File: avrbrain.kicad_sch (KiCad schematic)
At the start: 45 parts, among them J1 XKTF-0803-0, J12 PD/PE, J2 U254-051T-4BH81-S2S, J3 SM04B-SRSS-TB, J4 UPDI, J5 UEXT, J6 PIHAT, J7 PG/PB, J9 SM04B-SRSS-TB, Q1 BSS138, Q2 BSS138, SW1 RESET, U1 CH340C, U2 AVR128DB64x-xPT, U3 PCF8563T, U5 AMS1117-3.3, Y1 32kHz

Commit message: Tweaks to layout, finish all connections
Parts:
- removed J3: SM04B-SRSS-TB, Custom:JST_SM04B-SRSS-TB_LF__SN_, symbol Connector_Generic:Conn_01x04
- removed J6: PIHAT, Connector_PinHeader_2.54mm:PinHeader_2x13_P2.54mm_Vertical, symbol Connector_Generic:Conn_02x13_Odd_Even
- removed Q2: BSS138, Package_TO_SOT_SMD:SOT-23, symbol Transistor_FET:BSS138
- removed R2: 100K, Resistor_SMD:R_0402_1005Metric, symbol Device:R_Small
- removed Y1: 32kHz, Crystal:Crystal_SMD_3215-2Pin_3.2x1.5mm, symbol Device:Crystal_Small
- added J6: PC, Connector_PinHeader_2.54mm:PinHeader_2x10_P2.54mm_Vertical, symbol Connector_Generic:Conn_02x10_Odd_Even
- added J8: PG, Connector_PinHeader_2.54mm:PinHeader_2x10_P2.54mm_Vertical, symbol Connector_Generic:Conn_02x10_Odd_Even
- added JP1: AUTORESET, Jumper:SolderJumper-2_P1.3mm_Bridged_Pad1.0x1.5mm, symbol Jumper:Jumper_2_Bridged
- added JP2: CLK32K, Jumper:SolderJumper-2_P1.3mm_Bridged_Pad1.0x1.5mm, symbol Jumper:Jumper_2_Bridged
- added JP3: RTCINT, Jumper:SolderJumper-2_P1.3mm_Bridged_Pad1.0x1.5mm, symbol Jumper:Jumper_2_Bridged
- added SW2: VDD, SamacSys_Parts:JS202011CQN, symbol Switch:SW_SPDT
- J12: now not fitted
- J7: value PG/PB -> PA/PB; now not fitted
- renumbered D3 to D2, D2 to D3
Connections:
- net +3.3V: now also D2.2 (A), J1.P4 (VDD), J6.1 (Pin_1), J6.19 (Pin_19), SW2.3 (C), SW2.6 (C); no longer J1.P5 (CLK)
- net +5V: now also SW2.1 (A), SW2.4 (A)
- net CLK32K: now also JP2.1 (A); no longer U3.7 (CLKO)
- net GND: now also C6.2, J1.P6 (VSS), J4.3 (Pin_3), J6.10 (Pin_10), J6.12 (Pin_12), J6.14 (Pin_14), J6.16 (Pin_16), J6.18 (Pin_18), J6.2 (Pin_2), J6.20 (Pin_20), J6.4 (Pin_4), J6.6 (Pin_6), J6.8 (Pin_8), J8.10 (Pin_10), J8.12 (Pin_12), J8.14 (Pin_14), J8.16 (Pin_16), J8.18 (Pin_18), J8.2 (Pin_2), J8.20 (Pin_20), J8.4 (Pin_4), J8.6 (Pin_6), J8.8 (Pin_8); no longer J1.P7 (DAT0)
- net MISO: now also J1.P7 (DAT0), J6.11 (Pin_11); no longer J1.P8 (DAT1)
- net MOSI: now also J1.P3 (CMD), J6.13 (Pin_13); no longer J1.P4 (VDD)
- net PG0: now also J8.3 (Pin_3); no longer J7.4 (Pin_4)
- net PG1: now also J8.5 (Pin_5); no longer J7.6 (Pin_6)
- net PG2: now also J8.7 (Pin_7); no longer J7.8 (Pin_8)
- net PG3: now also J8.9 (Pin_9); no longer J7.10 (Pin_10)
- net PG4: now also J8.11 (Pin_11); no longer J7.12 (Pin_12)
- net PG5: now also J8.13 (Pin_13); no longer J7.14 (Pin_14)
- net PG6: now also J8.15 (Pin_15); no longer J7.16 (Pin_16)
- net PG7: now also J8.17 (Pin_17); no longer J7.18 (Pin_18)
- net RX3V: now also J6.5 (Pin_5)
- net SCK: now also J1.P5 (CLK), J6.15 (Pin_15); no longer J1.P6 (VSS)
- net TX3V: now also J6.3 (Pin_3)
- net VDD: now also C6.1, J4.2 (Pin_2), J8.1 (Pin_1), J8.19 (Pin_19), SW2.2 (B), SW2.5 (B); no longer D2.2 (A)
- net ~{CTS}: now also U2.47 (PF3); no longer U2.1 (PA3)
- net ~{DTR}: now also C8.1
- net ~{RTCINT}: now also U2.45 (XTAL32K2/PF1), JP3.1 (A); no longer U3.3 (~{INT})
- net ~{RTS}: no longer U2.64 (PA2)
- net ~{SDCS}: now also U2.46 (PF2); no longer U2.49 (PF5)
- net ~{UXCS}: now also J6.17 (Pin_17)
- net at Q1.2 (S), R1.1, R4.2: now also J1.P2 (DAT3/CD); no longer J1.P3 (CMD)
- net at J4.1 (Pin_1), SW1.2, U2.50 (~{RESET}/PF6): now also JP1.2 (B)
- net PA1: now reaches U2.63 (XTALHF2/PA1)
- net PA1: now also J7.6 (Pin_6)
- net PA0: now reaches U2.62 (XTALHF1/PA0)
- net PA0: now also J7.4 (Pin_4)
- net PA6: now reaches U2.4 (PA6)
- net PA6: now also J7.16 (Pin_16)
- net PA7: now reaches U2.5 (PA7)
- net PA7: now also J7.18 (Pin_18)
- net at C8.2: now also JP1.1 (A)
- net RX5V renamed PA4
- net PA4: now also J7.12 (Pin_12); no longer U1.2 (TXD)
- net SCL3V renamed SCL
- net SCL: now also U3.6 (SCL), J6.7 (Pin_7)
- removed net SCL5V: U2.46 (PF2), U3.6 (SCL)
- net SDA3V renamed SDA
- net SDA: now also U3.5 (SDA), J6.9 (Pin_9)
- removed net SDA5V: U2.47 (PF3), U3.5 (SDA)
- net TX5V renamed PA5
- net PA5: now also J7.14 (Pin_14); no longer U1.3 (RXD)
- net ~{DCD}: no longer names the net of U1.12 (~{DCD})
- net ~{DSR}: no longer names the net of U1.10 (~{DSR})
- net ~{PHCS} renamed RXU
- net RXU: now also U1.2 (TXD)
- net ~{RI}: no longer names the net of U1.11 (~{RI})
- new net: JP3.2 (B), U3.3 (~{INT})
- new net: JP2.2 (B), U3.7 (CLKO)
- new net PA2: J7.8 (Pin_8), U2.64 (PA2)
- new net PA3: J7.10 (Pin_10), U2.1 (PA3)
- new net TXU: U1.3 (RXD), U2.49 (PF5)
- no-connect marks 25 -> 16
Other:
- moved on the sheet: BT1, C1, C10, C2, C3, C8, C9, D2, D3, H1, H2, H3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

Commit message: Finish layout and routing
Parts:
- removed BT1: CR1216, Battery:BatteryHolder_Keystone_3001_1x12mm, symbol Device:Battery_Cell
- removed C1: 27pf, Capacitor_SMD:C_0603_1608Metric, symbol Device:C_Small
- removed C10, C9: 1uf, Capacitor_SMD:C_1206_3216Metric, symbol Device:C_Small
- removed C3 (x2), C5, C8: 0.1uf, Capacitor_SMD:C_0402_1005Metric, symbol Device:C_Small
- removed D1: LED, LED_SMD:LED_0805_2012Metric, symbol Device:LED
- removed D2, D3: 1N5819WS, Diode_SMD:D_SOD-323_HandSoldering, symbol Device:D_Small
- removed J1: XKTF-0803-0, SamacSys_Parts:XKTF08030, symbol Connector:Micro_SD_Card_Det1
- removed J12: PD/PE, Connector_PinHeader_2.54mm:PinHeader_2x20_P2.54mm_Vertical, symbol Connector_Generic:Conn_02x20_Odd_Even
- removed J2: U254-051T-4BH81-S2S, SamacSys_Parts:U254051T4BH81S2S, symbol Connector:USB_B_Micro
- removed J5: UEXT, Connector_IDC:IDC-Header_2x05_P2.54mm_Horizontal, symbol Connector_Generic:Conn_02x05_Odd_Even
- removed J6: PC, Connector_PinHeader_2.54mm:PinHeader_2x10_P2.54mm_Vertical, symbol Connector_Generic:Conn_02x10_Odd_Even
- removed J7: PA/PB, Connector_PinHeader_2.54mm:PinHeader_2x20_P2.54mm_Vertical, symbol Connector_Generic:Conn_02x20_Odd_Even
- removed J8: PG, Connector_PinHeader_2.54mm:PinHeader_2x10_P2.54mm_Vertical, symbol Connector_Generic:Conn_02x10_Odd_Even
- removed J9: SM04B-SRSS-TB, Custom:JST_SM04B-SRSS-TB_LF__SN_, symbol Connector_Generic:Conn_01x04
- removed JP1: AUTORESET, Jumper:SolderJumper-2_P1.3mm_Bridged_Pad1.0x1.5mm, symbol Jumper:Jumper_2_Bridged
- removed JP2: CLK32K, Jumper:SolderJumper-2_P1.3mm_Bridged_Pad1.0x1.5mm, symbol Jumper:Jumper_2_Bridged
- removed JP3: RTCINT, Jumper:SolderJumper-2_P1.3mm_Bridged_Pad1.0x1.5mm, symbol Jumper:Jumper_2_Bridged
- removed NT1: NetTie_2, NetTie:NetTie-2_SMD_Pad0.5mm, symbol Device:NetTie_2
- removed Q1: BSS138, Package_TO_SOT_SMD:SOT-23, symbol Transistor_FET:BSS138
- removed R1: 1K, Resistor_SMD:R_0402_1005Metric, symbol Device:R_Small
- removed R3, R4, R5, R6: 100K, Resistor_SMD:R_0402_1005Metric, symbol Device:R_Small
- removed SW2: VDD, SamacSys_Parts:JS202011CQN, symbol Switch:SW_SPDT
- removed U1: CH340C, Package_SO:SOIC-16_3.9x9.9mm_P1.27mm, symbol Interface_USB:CH340C
- removed U2: AVR128DB64x-xPT, Package_QFP:TQFP-64_10x10mm_P0.5mm, symbol MCU_Microchip_AVR_Dx:AVR128DB64x-xPT
- removed U3: PCF8563T, Package_SO:SOIC-8_3.9x4.9mm_P1.27mm, symbol Timer_RTC:PCF8563T
- removed U5: AMS1117-3.3, Package_TO_SOT_SMD:SOT-223-3_TabPin2, symbol Regulator_Linear:AMS1117-3.3
- removed Y1: 32kHz, Crystal:Crystal_SMD_3215-2Pin_3.2x1.5mm, symbol Device:Crystal_Small
- added C12, C7: 1uf, Capacitor_SMD:C_1206_3216Metric, symbol Device:C_Small
- added C15, C6: 22uf, Capacitor_SMD:C_1206_3216Metric, symbol Device:C_Small
- added J2: PORTD, Connector_PinSocket_2.54mm:PinSocket_2x09_P2.54mm_Vertical, symbol Connector_Generic:Conn_02x09_Odd_Even
- added J3: PORTG, Connector_PinSocket_2.54mm:PinSocket_2x09_P2.54mm_Vertical, symbol Connector_Generic:Conn_02x09_Odd_Even
- added J4: PORTE, Connector_PinSocket_2.54mm:PinSocket_2x09_P2.54mm_Vertical, symbol Connector_Generic:Conn_02x09_Odd_Even
- added J5: PORTA, Connector_PinSocket_2.54mm:PinSocket_2x09_P2.54mm_Vertical, symbol Connector_Generic:Conn_02x09_Odd_Even
- added J6: PORTB, Connector_PinSocket_2.54mm:PinSocket_2x09_P2.54mm_Vertical, symbol Connector_Generic:Conn_02x09_Odd_Even
- added J7: PORTC, Connector_PinSocket_2.54mm:PinSocket_2x09_P2.54mm_Vertical, symbol Connector_Generic:Conn_02x09_Odd_Even
- added JP4: VDD_MAIN, Jumper:SolderJumper-3_P1.3mm_Bridged2Bar12_RoundedPad1.0x1.5mm, symbol Jumper:Jumper_3_Bridged12
- added JP5: VDD_MVIO, Jumper:SolderJumper-3_P1.3mm_Bridged2Bar12_RoundedPad1.0x1.5mm, symbol Jumper:Jumper_3_Bridged12
- added U1: AVR128DB64x-xPT, Package_QFP:TQFP-64_10x10mm_P0.5mm, symbol MCU_Microchip_AVR_Dx:AVR128DB64x-xPT
- added U2: AMS1117-3.3, Package_TO_SOT_SMD:SOT-223-3_TabPin2, symbol Regulator_Linear:AMS1117-3.3
- renumbered C6 to C1, C3 to C2, C2 to C3, C1 to C4, C4 to C5, J4 to J1
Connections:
- net +3.3V: now also C12.1, C15.1, JP4.3 (B), JP5.1 (A), U2.2 (VO); no longer C5.1
- net +5V: now also C6.1, C7.1, JP4.1 (A), JP5.3 (B), U2.3 (VI)
- net CLK32K: now also U1.44 (XTAL32K1/PF0)
- net GND: now also C12.2, C15.2, C6.2, C7.2, J2.10 (Pin_10), J2.12 (Pin_12), J2.14 (Pin_14), J2.16 (Pin_16), J2.18 (Pin_18), J2.2 (Pin_2), J2.4 (Pin_4), J2.6 (Pin_6), J2.8 (Pin_8), J3.10 (Pin_10), J3.12 (Pin_12), J3.14 (Pin_14), J3.16 (Pin_16), J3.18 (Pin_18), J3.2 (Pin_2), J3.4 (Pin_4), J3.6 (Pin_6), J3.8 (Pin_8), J4.10 (Pin_10), J4.12 (Pin_12), J4.14 (Pin_14), J4.16 (Pin_16), J4.18 (Pin_18), J4.2 (Pin_2), J4.4 (Pin_4), J4.6 (Pin_6), J4.8 (Pin_8), J5.10 (Pin_10), J5.12 (Pin_12), J5.14 (Pin_14), J5.16 (Pin_16), J5.18 (Pin_18), J5.2 (Pin_2), J5.4 (Pin_4), J5.6 (Pin_6), J5.8 (Pin_8), J6.10 (Pin_10), J6.12 (Pin_12), J6.14 (Pin_14), J6.16 (Pin_16), J6.18 (Pin_18), J6.2 (Pin_2), J6.4 (Pin_4), J6.6 (Pin_6), J6.8 (Pin_8), J7.10 (Pin_10), J7.12 (Pin_12), J7.14 (Pin_14), J7.16 (Pin_16), J7.18 (Pin_18), J7.2 (Pin_2), J7.4 (Pin_4), J7.6 (Pin_6), J7.8 (Pin_8), U1.21 (GND), U1.35 (AGND), U1.57 (GND), U1.7 (GND), U2.1 (GND)
- net MISO: now also J7.11 (Pin_11), U1.22 (PC4)
- net MOSI: now also J7.13 (Pin_13), U1.23 (PC5)
- net PA0: now also J5.3 (Pin_3), U1.62 (XTALHF1/PA0)
- net PA1: now also J5.5 (Pin_5), U1.63 (XTALHF2/PA1)
- net PA2: now also J5.7 (Pin_7), U1.64 (PA2)
- net PA3: now also J5.9 (Pin_9), U1.1 (PA3)
- net PA4: now also J5.11 (Pin_11), U1.2 (PA4)
- net PA5: now also J5.13 (Pin_13), U1.3 (PA5)
- net PA6: now also J5.15 (Pin_15), U1.4 (PA6)
- net PA7: now also J5.17 (Pin_17), U1.5 (PA7)
- net PB0: now also J6.3 (Pin_3), U1.8 (PB0)
- net PB1: now also J6.5 (Pin_5), U1.9 (PB1)
- net PB2: now also J6.7 (Pin_7), U1.10 (PB2)
- net PB3: now also J6.9 (Pin_9), U1.11 (PB3)
- net PB4: now also J6.11 (Pin_11), U1.12 (PB4)
- net PB5: now also J6.13 (Pin_13), U1.13 (PB5)
- net PB6: now also J6.15 (Pin_15), U1.14 (PB6)
- net PB7: now also J6.17 (Pin_17), U1.15 (PB7)
- net PD0: now also J2.3 (Pin_3), U1.26 (PD0)
- net PD1: now also J2.5 (Pin_5), U1.27 (PD1)
- net PD2: now also J2.7 (Pin_7), U1.28 (PD2)
- net PD3: now also J2.9 (Pin_9), U1.29 (PD3)
- net PD4: now also J2.11 (Pin_11), U1.30 (PD4)
- net PD5: now also J2.13 (Pin_13), U1.31 (PD5)
- net PD6: now also J2.15 (Pin_15), U1.32 (PD6)
- net PD7: now also J2.17 (Pin_17), U1.33 (VREFA/PD7)
- net PE0: now also J4.3 (Pin_3), U1.36 (PE0)
- net PE1: now also J4.5 (Pin_5), U1.37 (PE1)
- net PE2: now also J4.7 (Pin_7), U1.38 (PE2)
- net PE3: now also J4.9 (Pin_9), U1.39 (PE3)
- net PE4: now also J4.11 (Pin_11), U1.40 (PE4)
- net PE5: now also J4.13 (Pin_13), U1.41 (PE5)
- net PE6: now also J4.15 (Pin_15), U1.42 (PE6)
- net PE7: now also J4.17 (Pin_17), U1.43 (PE7)
- net PG0: now also J3.3 (Pin_3), U1.52 (PG0)
- net PG1: now also J3.5 (Pin_5), U1.53 (PG1)
- net PG2: now also J3.7 (Pin_7), U1.54 (PG2)
- net PG3: now also J3.9 (Pin_9), U1.55 (PG3)
- net PG4: now also J3.11 (Pin_11), U1.58 (PG4)
- net PG5: now also J3.13 (Pin_13), U1.59 (PG5)
- net PG6: now also J3.15 (Pin_15), U1.60 (PG6)
- net PG7: now also J3.17 (Pin_17), U1.61 (PG7)
- net SCK: now also J7.15 (Pin_15), U1.24 (PC6)
- net SCL: now also J7.9 (Pin_9), U1.19 (PC3)
- net SDA: now also J7.7 (Pin_7), U1.18 (PC2)
- net VDD: now also J2.1 (Pin_1), J3.1 (Pin_1), J4.1 (Pin_1), J5.1 (Pin_1), J6.1 (Pin_1), JP4.2 (C), U1.34 (AVDD), U1.56 (VDD), U1.6 (VDD)
- net ~{CTS}: now also U1.47 (PF3)
- net ~{RTCINT}: now also U1.45 (XTAL32K2/PF1)
- net ~{SDCS}: now also U1.46 (PF2)
- net UPDI: now reaches J1.1 (Pin_1)
- net UPDI: now also U1.51 (UPDI); no longer SW1.2
- net ~{RESET}: now reaches J1.4 (Pin_4)
- net ~{RESET}: now also SW1.2, U1.50 (~{RESET}/PF6)
- new net RXC: J7.5 (Pin_5), U1.17 (PC1)
- new net RXF: U1.48 (PF4)
- new net TXC: J7.3 (Pin_3), U1.16 (PC0)
- new net TXF: U1.49 (PF5)
- new net VDDF: C5.1, J7.1 (Pin_1), JP5.2 (C), U1.20 (VDDIO2)
- new net ~{CS}: J7.17 (Pin_17), U1.25 (PC7)
- no-connect marks 16 -> 0
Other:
- added sheet Peripherals (peripherals.kicad_sch)
- title: z80ctrl NG -> AVRbrain
- moved on the sheet: C1, C2, C3, C4, C5, H1, H2, H3, H4, J1, SW1

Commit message: Final touches
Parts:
- added C16, C17: 1uf, Capacitor_SMD:C_1206_3216Metric, symbol Device:C_Small
- added J10: PORTF, Connector_PinSocket_2.54mm:PinSocket_1x02_P2.54mm_Vertical, symbol Connector_Generic:Conn_01x02
- J2, J3, J4, J5, J6, J7: now not fitted
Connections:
- net CLK32K: now also J10.2 (Pin_2)
- net GND: now also C16.1, C17.2
- net RXF: now also U1.49 (PF5); no longer U1.48 (PF4)
- net TXF: now also U1.48 (PF4); no longer U1.49 (PF5)
- net VDD: now also C16.2
- net VDDF: now also C17.1
- net ~{RTCINT}: now also J10.1 (Pin_1)
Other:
- moved on the sheet: C1, C2, C3, C4, C5, J1, JP4, JP5, SW1, U1

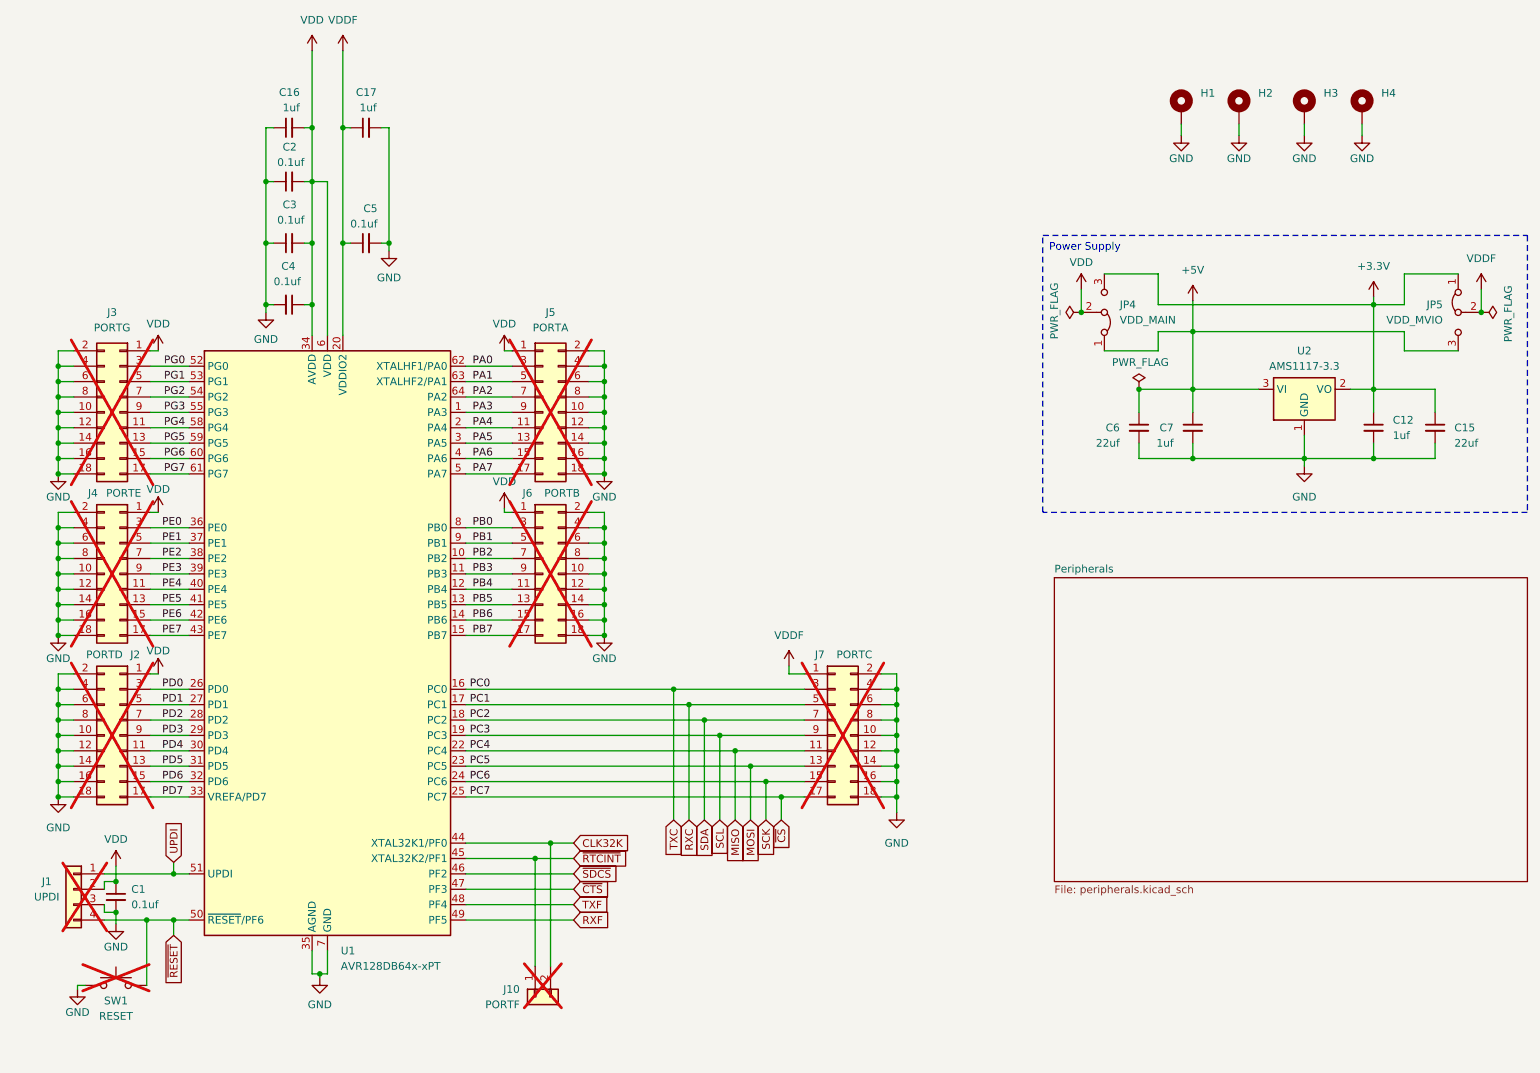
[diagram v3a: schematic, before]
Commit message: Switch to 4 layer; reduce connector size and move to edge
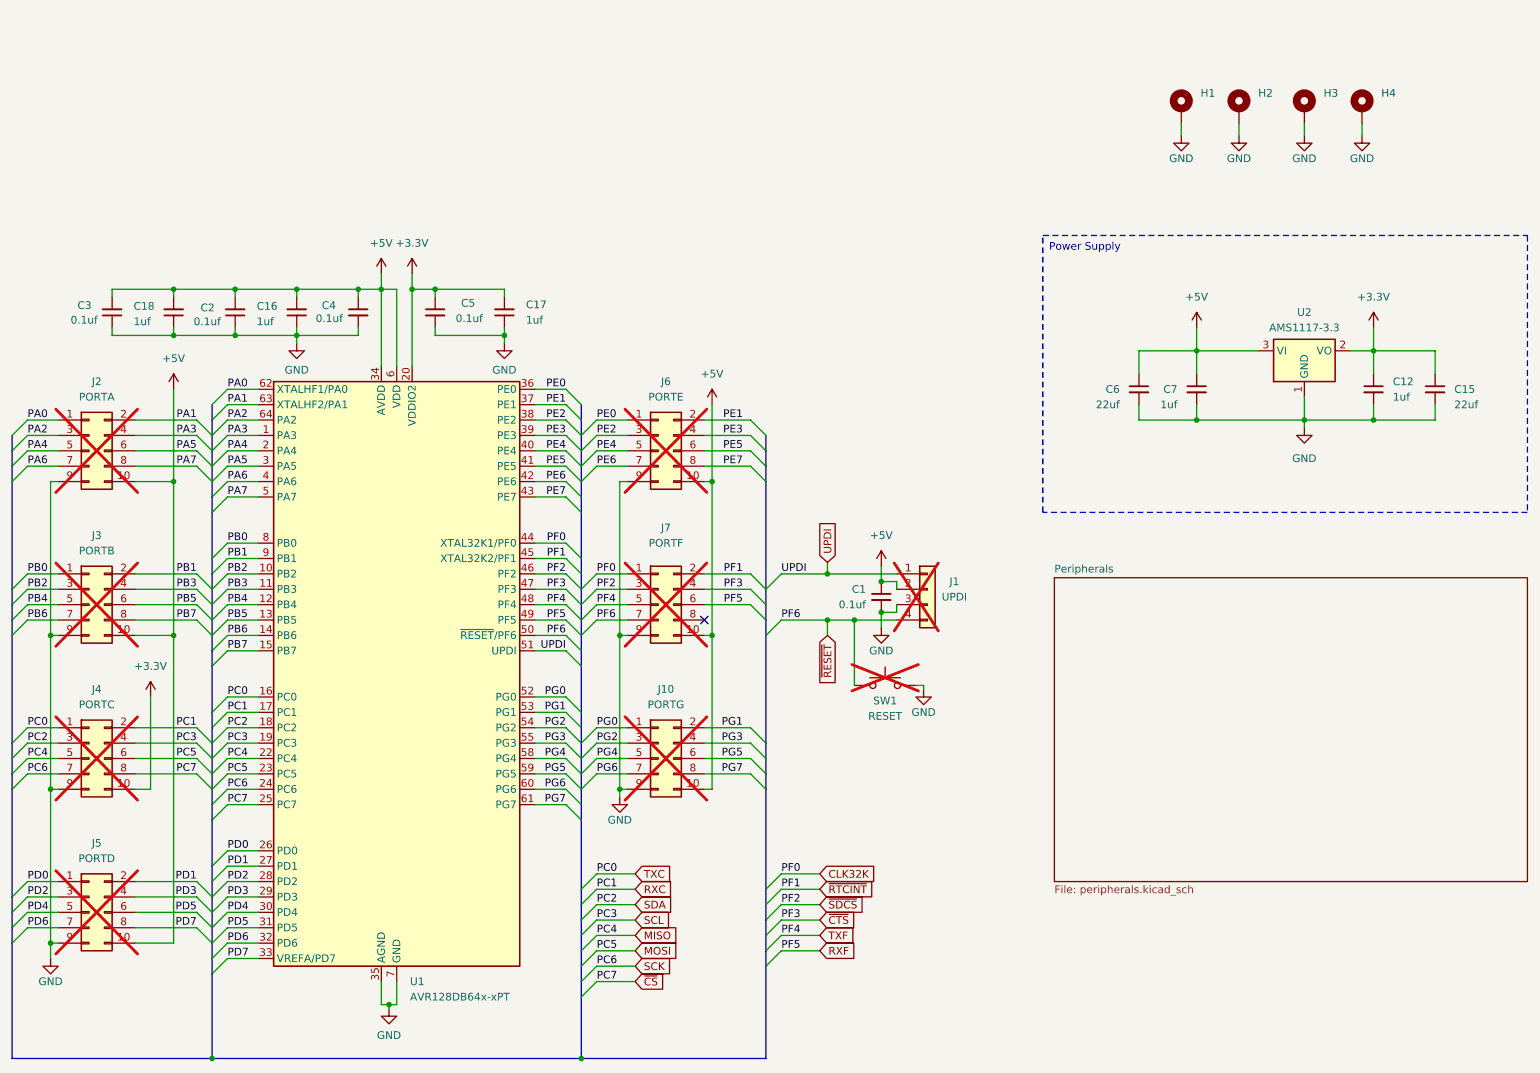
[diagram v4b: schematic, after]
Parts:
- removed J10: PORTF, Connector_PinSocket_2.54mm:PinSocket_1x02_P2.54mm_Vertical, symbol Connector_Generic:Conn_01x02
- removed J2: PORTD, Connector_PinSocket_2.54mm:PinSocket_2x09_P2.54mm_Vertical, symbol Connector_Generic:Conn_02x09_Odd_Even
- removed J3: PORTG, Connector_PinSocket_2.54mm:PinSocket_2x09_P2.54mm_Vertical, symbol Connector_Generic:Conn_02x09_Odd_Even
- removed J4: PORTE, Connector_PinSocket_2.54mm:PinSocket_2x09_P2.54mm_Vertical, symbol Connector_Generic:Conn_02x09_Odd_Even
- removed J5: PORTA, Connector_PinSocket_2.54mm:PinSocket_2x09_P2.54mm_Vertical, symbol Connector_Generic:Conn_02x09_Odd_Even
- removed J6: PORTB, Connector_PinSocket_2.54mm:PinSocket_2x09_P2.54mm_Vertical, symbol Connector_Generic:Conn_02x09_Odd_Even
- removed J7: PORTC, Connector_PinSocket_2.54mm:PinSocket_2x09_P2.54mm_Vertical, symbol Connector_Generic:Conn_02x09_Odd_Even
- removed JP4: VDD_MAIN, Jumper:SolderJumper-3_P1.3mm_Bridged2Bar12_RoundedPad1.0x1.5mm, symbol Jumper:Jumper_3_Bridged12
- removed JP5: VDD_MVIO, Jumper:SolderJumper-3_P1.3mm_Bridged2Bar12_RoundedPad1.0x1.5mm, symbol Jumper:Jumper_3_Bridged12
- added C18: 1uf, Capacitor_SMD:C_1206_3216Metric, symbol Device:C_Small
- added J10: PORTG, Connector_PinHeader_2.54mm:PinHeader_2x05_P2.54mm_Vertical, symbol Connector_Generic:Conn_02x05_Odd_Even
- added J2: PORTA, Connector_PinHeader_2.54mm:PinHeader_2x05_P2.54mm_Vertical, symbol Connector_Generic:Conn_02x05_Odd_Even
- added J3: PORTB, Connector_PinHeader_2.54mm:PinHeader_2x05_P2.54mm_Vertical, symbol Connector_Generic:Conn_02x05_Odd_Even
- added J4: PORTC, Connector_PinHeader_2.54mm:PinHeader_2x05_P2.54mm_Vertical, symbol Connector_Generic:Conn_02x05_Odd_Even
- added J5: PORTD, Connector_PinHeader_2.54mm:PinHeader_2x05_P2.54mm_Vertical, symbol Connector_Generic:Conn_02x05_Odd_Even
- added J6: PORTE, Connector_PinHeader_2.54mm:PinHeader_2x05_P2.54mm_Vertical, symbol Connector_Generic:Conn_02x05_Odd_Even
- added J7: PORTF, Connector_PinHeader_2.54mm:PinHeader_2x05_P2.54mm_Vertical, symbol Connector_Generic:Conn_02x05_Odd_Even
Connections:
- net VDD is gone; now on net +5V: C1.1, C16.2, C2.2, C3.2, C4.1, J1.2 (Pin_2), U1.34 (AVDD), U1.56 (VDD), U1.6 (VDD)
- net +3.3V: now also C17.2, C5.1, U1.20 (VDDIO2), J4.10 (Pin_10)
- net +5V: now also C18.2, J10.10 (Pin_10), J2.10 (Pin_10), J3.10 (Pin_10), J5.10 (Pin_10), J6.10 (Pin_10), J7.10 (Pin_10)
- net CLK32K: now also J7.1 (Pin_1)
- net GND: now also C17.1, C18.1, J10.9 (Pin_9), J2.9 (Pin_9), J3.9 (Pin_9), J4.9 (Pin_9), J5.9 (Pin_9), J6.9 (Pin_9), J7.9 (Pin_9); no longer C17.2
- net MISO: now also J4.5 (Pin_5)
- net MOSI: now also J4.6 (Pin_6)
- net PA0: now also J2.1 (Pin_1)
- net PA1: now also J2.2 (Pin_2)
- net PA2: now also J2.3 (Pin_3)
- net PA3: now also J2.4 (Pin_4)
- net PA4: now also J2.5 (Pin_5)
- net PA5: now also J2.6 (Pin_6)
- net PA6: now also J2.7 (Pin_7)
- net PA7: now also J2.8 (Pin_8)
- net PB0: now also J3.1 (Pin_1)
- net PB1: now also J3.2 (Pin_2)
- net PB2: now also J3.3 (Pin_3)
- net PB3: now also J3.4 (Pin_4)
- net PB4: now also J3.5 (Pin_5)
- net PB5: now also J3.6 (Pin_6)
- net PB6: now also J3.7 (Pin_7)
- net PB7: now also J3.8 (Pin_8)
- net PD0: now also J5.1 (Pin_1)
- net PD1: now also J5.2 (Pin_2)
- net PD2: now also J5.3 (Pin_3)
- net PD3: now also J5.4 (Pin_4)
- net PD4: now also J5.5 (Pin_5)
- net PD5: now also J5.6 (Pin_6)
- net PD6: now also J5.7 (Pin_7)
- net PD7: now also J5.8 (Pin_8)
- net PE0: now also J6.1 (Pin_1)
- net PE1: now also J6.2 (Pin_2)
- net PE2: now also J6.3 (Pin_3)
- net PE3: now also J6.4 (Pin_4)
- net PE4: now also J6.5 (Pin_5)
- net PE5: now also J6.6 (Pin_6)
- net PE6: now also J6.7 (Pin_7)
- net PE7: now also J6.8 (Pin_8)
- net PG0: now also J10.1 (Pin_1)
- net PG1: now also J10.2 (Pin_2)
- net PG2: now also J10.3 (Pin_3)
- net PG3: now also J10.4 (Pin_4)
- net PG4: now also J10.5 (Pin_5)
- net PG5: now also J10.6 (Pin_6)
- net PG6: now also J10.7 (Pin_7)
- net PG7: now also J10.8 (Pin_8)
- net RXC: now also J4.2 (Pin_2)
- net RXF: now also J7.6 (Pin_6)
- net SCK: now also J4.7 (Pin_7)
- net SCL: now also J4.4 (Pin_4)
- net SDA: now also J4.3 (Pin_3)
- net TXC: now also J4.1 (Pin_1)
- net TXF: now also J7.5 (Pin_5)
- net ~{CS}: now also J4.8 (Pin_8)
- net ~{CTS}: now also J7.4 (Pin_4)
- net ~{RESET}: now also J7.7 (Pin_7)
- net ~{RTCINT}: now also J7.2 (Pin_2)
- net ~{SDCS}: now also J7.3 (Pin_3)
- removed net VDDF: C17.1, C5.1, U1.20 (VDDIO2)
- no-connect marks 0 -> 1
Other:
- moved on the sheet: C1, C12, C15, C16, C17, C2, C3, C4, C5, C6, C7, J1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

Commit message: Final (?!) tweaks
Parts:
- added C19: 1uf, Capacitor_SMD:C_1206_3216Metric, symbol Device:C_Small
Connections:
- net +5V: now also C19.2
- net GND: now also C19.1
